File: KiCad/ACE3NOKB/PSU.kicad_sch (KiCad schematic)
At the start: 37 parts, among them U1 LM7805_TO220

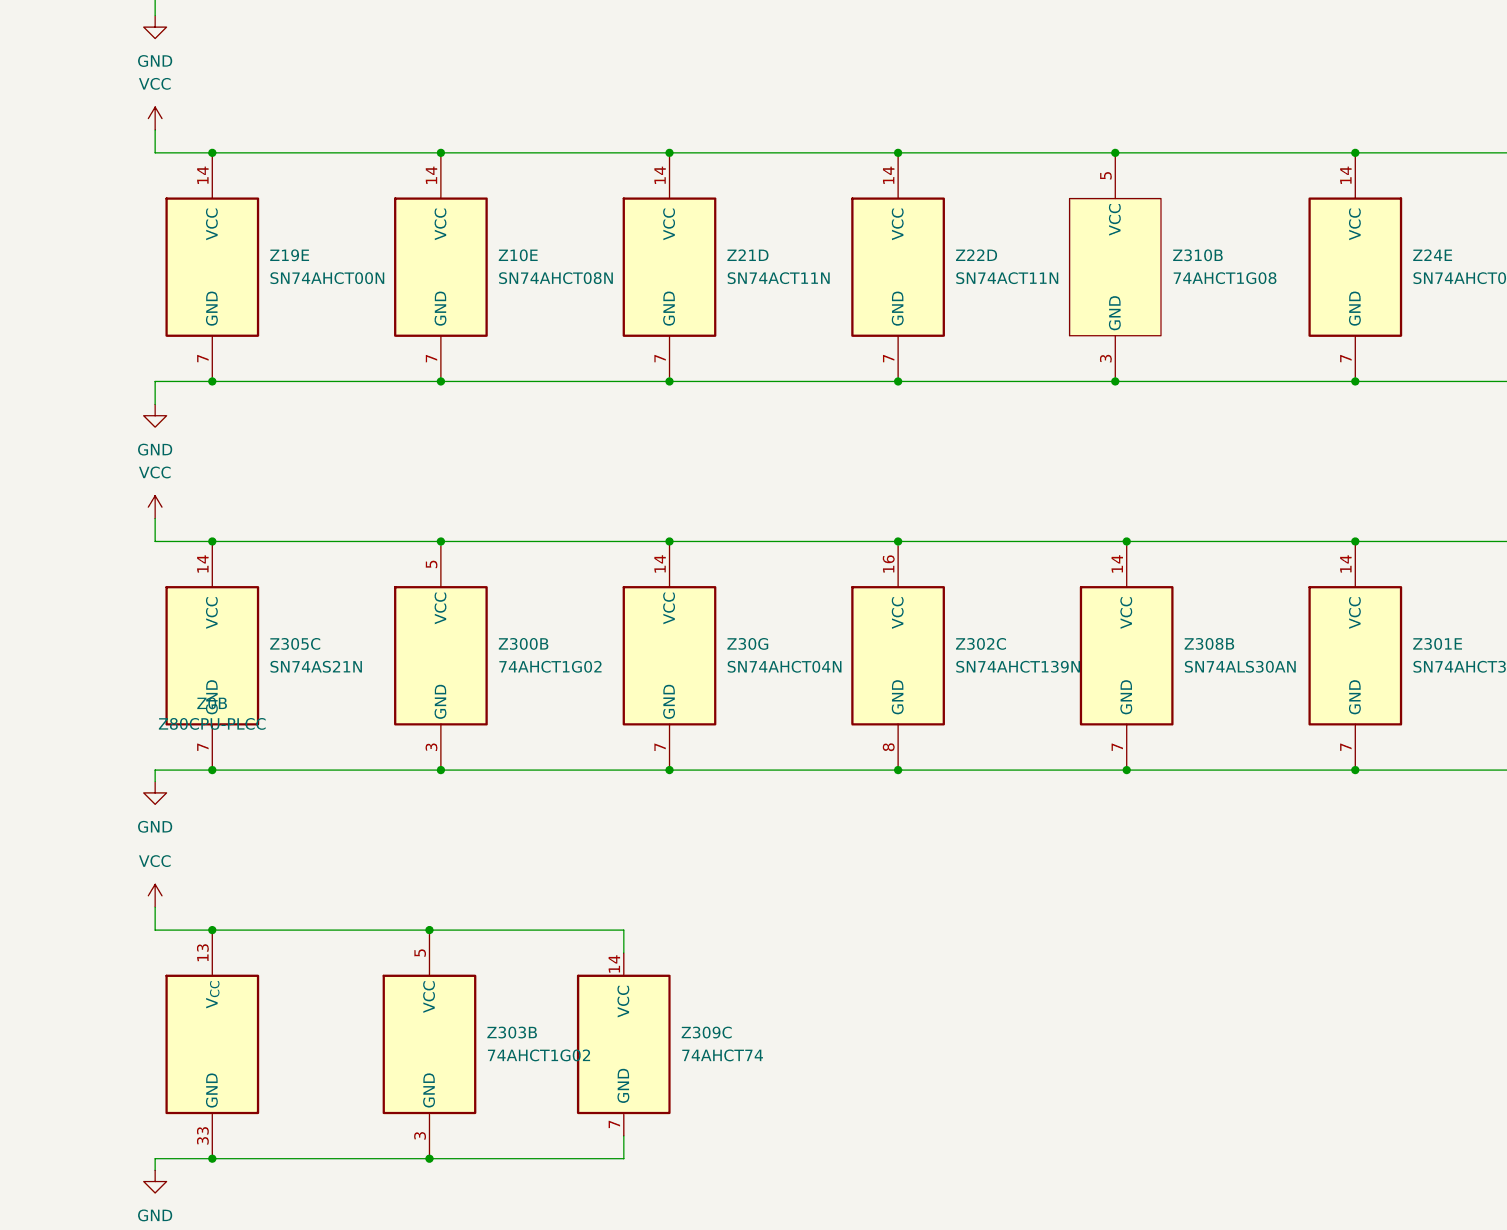
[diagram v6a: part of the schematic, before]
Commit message: Change Address decode to speed up the use of /WAIT to avoid conflicts when setting up character RAM. Rerange priority on Internal external /WAIT. Reconnect Clock to rest of circuit.
Signed-off-by: John Bradley <flypie@rocketmail.com>
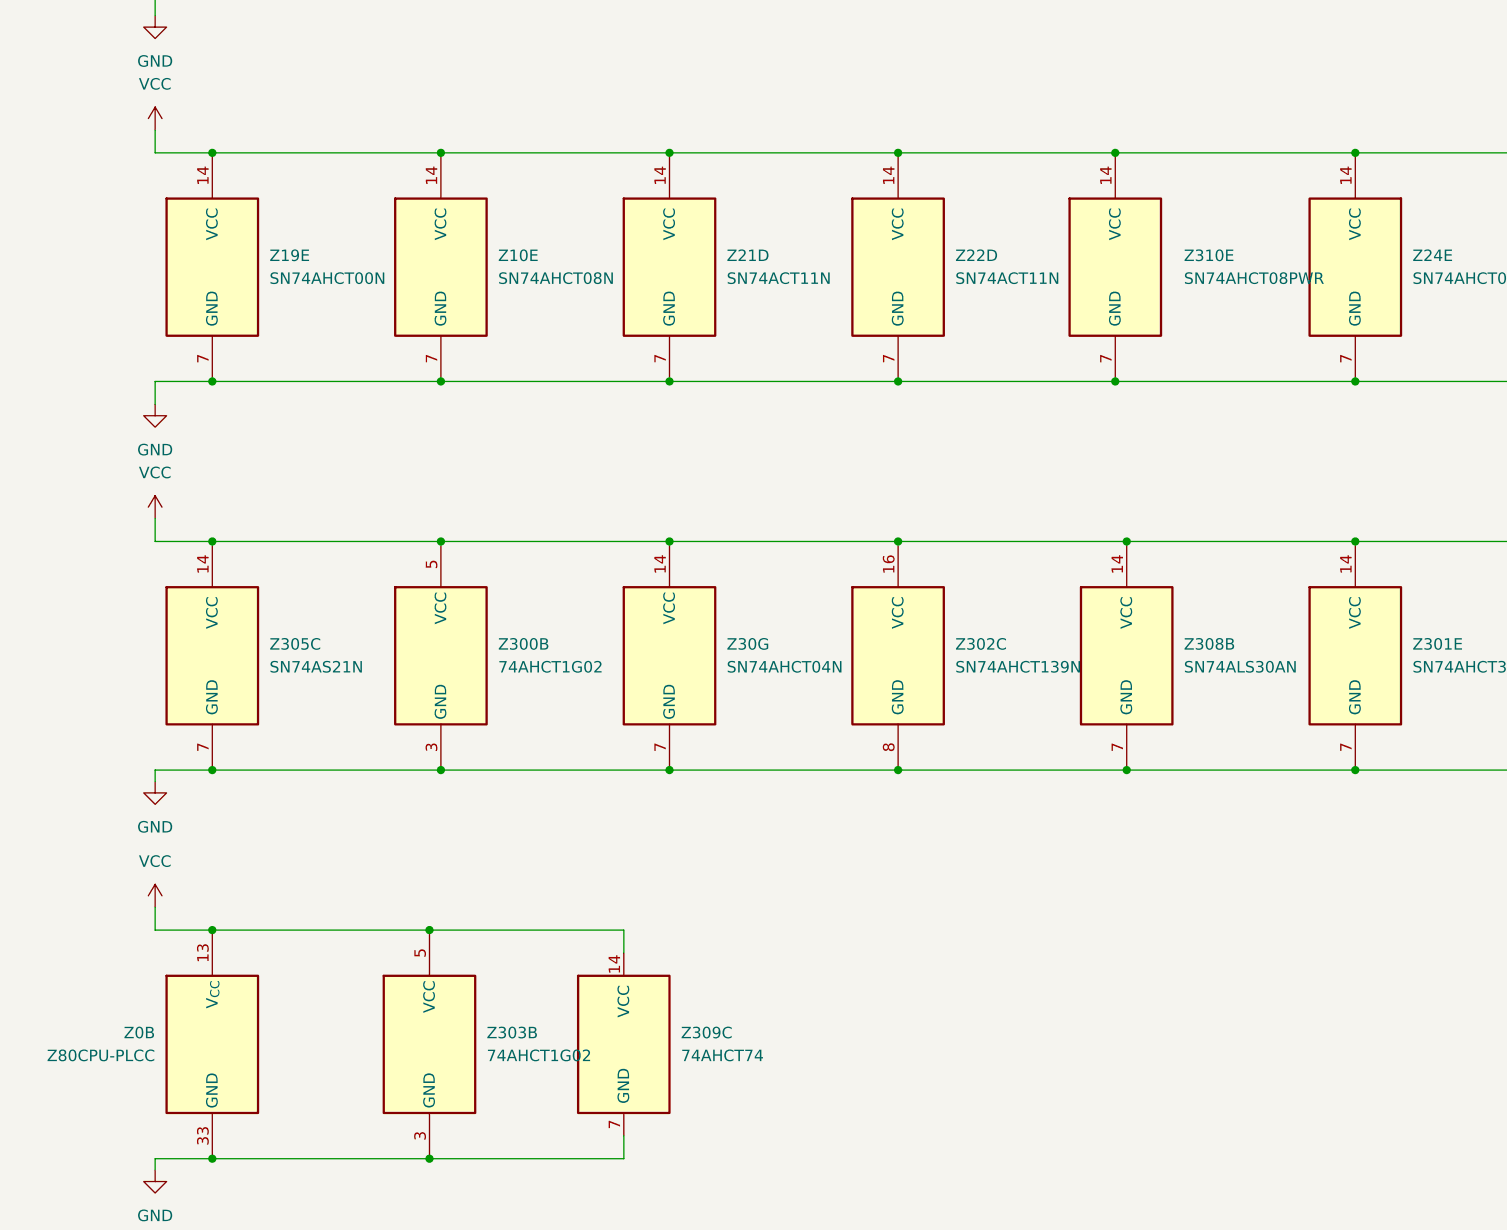
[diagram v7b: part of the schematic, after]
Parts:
- removed Z310: 74AHCT1G08, Package_TO_SOT_SMD:SOT-23-5, symbol MY74xGxx:74AHCT1G08
- added Z310: SN74AHCT08PWR, Package_SO:TSSOP-14_4.4x5mm_P0.65mm, symbol 74xx-FIX:74LS08
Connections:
- net GND: now also Z310.7 (GND)
- net VCC: now also Z310.14 (VCC)
